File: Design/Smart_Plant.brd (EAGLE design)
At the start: 80 x 129.1 mm, 96 parts, among them IC1 TP4056, IC2 TLC555CDR, IC3 AHT20, IC4 RT9080-33GJ5, IC5 LC709203F/MH, IC6 VEML7700-TR, J6 USB-C, Q1 IRLML0100, T1 MMBT2222A, T2 LBSS84LT1G, U2 ESP32-WROOM-32, X5 ESP32-S3QFN54, Y2 40MHz

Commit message: Design V1R3
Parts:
- removed C21: 5.6pF, esp32-thing-temp:0603
- removed C46, C48, C55, C57, C62, C63: 1uF, microbuilder:_0402NO
- removed C47, C52, C53, C54, C56, C58: 0.1uF, microbuilder:_0402NO
- removed C49: 22uF, microbuilder:0805-NO
- removed C59, C60: 16pF, microbuilder:_0402NO
- removed C61: 1uF, SpaceDIY_passive_components:C0402
- removed E2: ANTENNA, esp32-thing-temp:TRACE_ANTENNA_2.4GHZ_25.7MM_TUNED
- removed IC5: LC709203F/MH, adafruit_sensor:WLCSP9
- removed J4: (no value), SpaceDIY_connectors:JST-2-SMD
- removed L2: 2.7nH, SparkFun-Passives:0603
- removed L5: 2nH, microbuilder:_0402NO
- removed R29: 0, microbuilder:_0402NO
- removed R30: 1Meg, microbuilder:_0402NO
- removed R31: 10K, SpaceDIY_passive_components:R0402
- removed U$42: (no value), itsy_silks:QTPY_ESP32_TOP
- removed U2: ESP32-WROOM-32, ESP32-WROOM-32:MODULE_ESP32-WROOM-32
- removed X5: ESP32-S3QFN54, adafruit_wireless:QFN56_7X7
- removed Y2: 40MHz, microbuilder:CRYSTAL_2X1.6
- added C12: 0.1uF, rcl:C0603
- added IC7: MAX17048G+T10, SpaceDIY_IC:SON50P200X200X80-9N
- added R36, R37: 5.1k, rcl:R0603
- added R9: 10K, rcl:R0603
- added U1: ESP32-S3-MINI-1-N8, SpaceDIY_modules:XCVR_ESP32-S3-MINI-1-N8
- C20: value 2.4pF -> 10uF; device esp32-thing-temp:0603 -> rcl:C0603
- C40: value 1uF -> 0.1uF
- FPC: device SpaceDIY_connectors:FPC-05FB-24PH20 -> SpaceDIY_connectors:FPC_24_0.5MM
- J1: device SparkFun-Connectors:1X02 -> SpaceDIY_connectors:JST-2-SMD
- moved R18 146.9 mm to (25.5, 13.4), turned to 90 degrees
- moved R14 142.0 mm to (23.4, 13.6), turned to 270 degrees
- moved C20 58.3 mm to (25.5, 27.0), turned to 180 degrees
- moved C11 42.1 mm to (15.0, 30.0)
- moved C40 34.3 mm to (22.0, 17.5)
- moved J1 20.1 mm to (5.50, 17.0)
- moved C4 14.6 mm to (11.5, 17.5), turned to 90 degrees
- moved R6 12.1 mm to (3.50, 32.5)
- moved IC1 11.7 mm to (16.0, 19.5)
- moved R4 9.85 mm to (11.5, 21.0), turned to 270 degrees
- moved C8 9.69 mm to (14.0, 13.5), turned to 90 degrees
- moved C1 9.54 mm to (11.5, 13.5), turned to 90 degrees
- moved IC6 8.06 mm to (10.0, 32.5)
- moved R5 7.68 mm to (7.00, 32.5)
- moved IC4 6.21 mm to (17.5, 13.5), turned to 0 degrees
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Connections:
- removed net !RESET: C61.1, R31.2, S2.3, X5.4
- removed net A2: X5.14
- removed net A3: X5.13
- removed net IO10_DBLTAP: C62.1, R30.2, X5.15
- removed net LIGHT: U2.9
- removed net LNA_IN1: C21.1, L2.1, X5.1
- removed net MISO: X5.42
- removed net N$53: C59.1, X5.54, Y2.3
- removed net N$54: C60.1, R29.1, Y2.1
- removed net N$55: R29.2, X5.53
- removed net NEOPIX: X5.44
- removed net NEOPIX_PWR: X5.43
- removed net SCK: X5.41
- removed net SCL1: X5.45
- removed net SDA1: X5.47
- removed net TRACE_ANT1: C20.1, C21.2, E2.ANT
- removed net VDD3P3: C47.1, L5.2, X5.2, X5.3
- removed net VDD_SPI: C54.1, C55.1, X5.29
- new net +SOL: D6.A, R20.1
- new net N$35: J6.B5, R36.2
- net 3.3V: now also C12.1, C20.1, R9.2, U1.3; no longer C46.1, C48.1, C49.1, C52.1, C53.1, C56.1, C57.1, C58.1, C63.1, L5.1, R31.1, U2.2, X5.20, X5.27, X5.46, X5.55, X5.56
- net BATTERY: now also U1.21; no longer U2.7, X5.24
- net BUSY: now also U1.28; no longer U2.10
- net D+: now also U1.24; no longer X5.26
- net D-: now also U1.23; no longer X5.25
- net DC: now also U1.33; no longer U2.12
- net DISPCS: now also U1.29; no longer U2.23
- net GND: now also C12.2, IC7.1, IC7.4, IC7.6, IC7.9, R36.1, R37.1, U1.1, U1.2, U1.42, U1.43, U1.46, U1.47, U1.48, U1.49, U1.50, U1.51, U1.52, U1.53, U1.54, U1.55, U1.56, U1.57, U1.58, U1.59, U1.60, U1.61, U1.61_1, U1.61_2, U1.61_3, U1.61_4, U1.61_5, U1.61_6, U1.61_7, U1.61_8, U1.62, U1.63, U1.64, U1.65; no longer C46.2, C47.2, C48.2, C49.2, C52.2, C53.2, C54.2, C55.2, C56.2, C57.2, C58.2, C59.2, C60.2, C61.2, C62.2, C63.2, E2.GND, E2.GND2, IC5.A1, IC5.B1, J4.2, L2.2, R30.1, U2.1, U2.15, U2.38, U2.39_1, U2.39_10, U2.39_11, U2.39_12, U2.39_13, U2.39_14, U2.39_15, U2.39_16, U2.39_17, U2.39_18, U2.39_19, U2.39_2, U2.39_20, U2.39_21, U2.39_3, U2.39_4, U2.39_5, U2.39_6, U2.39_7, U2.39_8, U2.39_9, X5.57
- net IO0: now also U1.4; no longer U2.25, X5.5
- net MOISTURE: now also U1.19; no longer U2.8, X5.23
- net MOSI: now also U1.31; no longer U2.13, X5.40
- net N$46: now also J6.A5, R37.2; no longer D6.A, J1.1, R20.1
- net RESET: now also U1.34; no longer U2.11
- net RST: now also R9.1, S2.3, U1.45; no longer U2.3
- net RX: now also U1.40; no longer U2.34, X5.50
- net SCL: now also IC7.7, U1.8; no longer IC5.C2, U2.36, X5.11
- net SCLK: now also U1.32; no longer U2.16
- net SDA: now also IC7.8, U1.7; no longer IC5.C1, U2.33, X5.12
- net SENS: now also U1.25; no longer U2.27, X5.9
- net TX: now also U1.39; no longer U2.35, X5.49
- net VBAT: now also IC7.2, IC7.3, J1.1; no longer IC5.A3, J4.1
- net VSOLAR: now also U1.20; no longer U2.6
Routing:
- net VSENS: track 69.3 -> 125.7 mm, vias 4 -> 5
- net SCL: track 19.1 -> 64.3 mm, vias 0 -> 5
- net SDA: track 18.4 -> 61.7 mm, vias 0 -> 5
- net D+: track 0.00 -> 40.1 mm, vias 0 -> 2
- net D-: track 0.00 -> 39.3 mm, vias 0 -> 2
- net RST: track 59.5 -> 34.1 mm
- net N$1: track 2.86 -> 26.2 mm, vias 0 -> 2
- net N$6: track 2.29 -> 23.3 mm, vias 0 -> 2
- net DC: track 48.7 -> 30.8 mm
- net RESET: track 47.5 -> 29.7 mm
- net N$3: track 19.2 -> 2.00 mm, vias 2 -> 0
- net SCLK: track 42.5 -> 25.5 mm
- net MOSI: track 42.3 -> 25.3 mm
- net GND: track 12.3 -> 26.9 mm, vias 73 -> 40
- net VIN: track 48.7 -> 62.8 mm, vias 3 -> 4
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- added copper zone on layer 1, net +SOL
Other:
- board text added: "V1R3"
- board text removed: "+"
- board text removed: "-"
- board text removed: "V1R2"

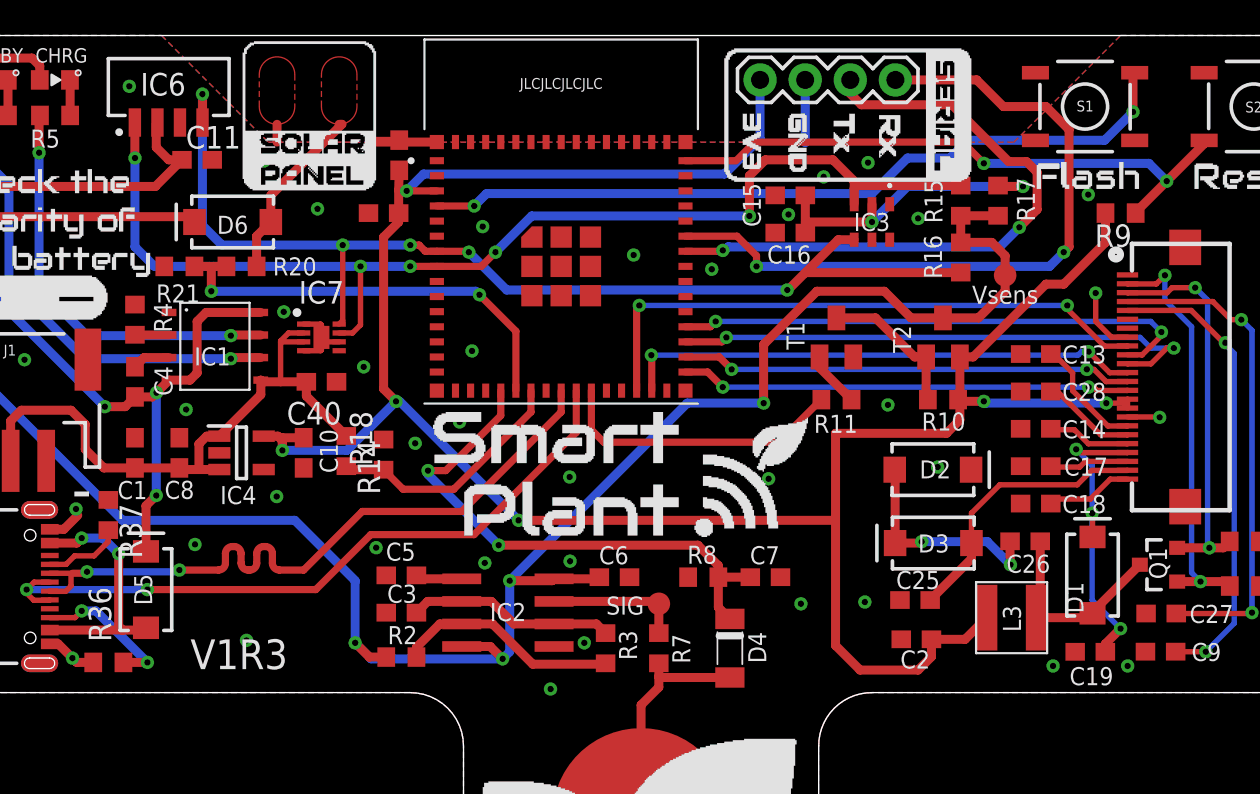
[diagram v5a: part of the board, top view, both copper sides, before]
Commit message: First draft of the V2R1 design
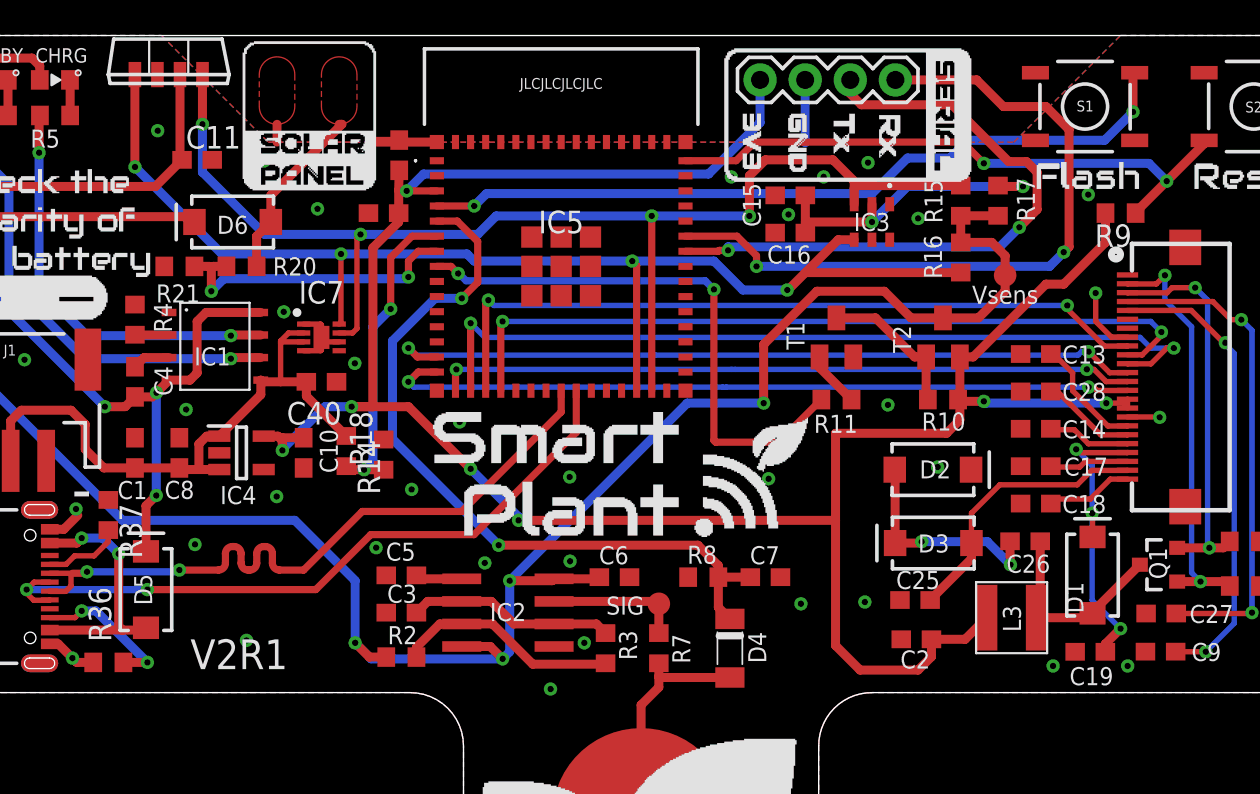
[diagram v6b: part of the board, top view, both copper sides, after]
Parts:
- removed U1: ESP32-S3-MINI-1-N8, SpaceDIY_modules:XCVR_ESP32-S3-MINI-1-N8
- added IC5: ESP32-S2-MINI-1-N4R2, SpaceDIY_modules:ESP32S2MINI1N4R2
- IC6: device SpaceDIY_sensors:VEML7700 -> SpaceDIY_sensors:VEML7700-TR
- moved IC6 2.00 mm to (10.0, 34.5)
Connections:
- net 3.3V: now also IC5.3; no longer U1.3
- net BATTERY: now also IC5.6; no longer U1.21
- net BUSY: now also IC5.18; no longer U1.28
- net D+: now also IC5.24; no longer U1.24
- net D-: now also IC5.23; no longer U1.23
- net DC: now also IC5.17; no longer U1.33
- net DISPCS: now also IC5.14; no longer U1.29
- net GND: now also IC5.1, IC5.2, IC5.30, IC5.42, IC5.43, IC5.46, IC5.47, IC5.48, IC5.49, IC5.50, IC5.51, IC5.52, IC5.53, IC5.54, IC5.55, IC5.56, IC5.57, IC5.58, IC5.59, IC5.60, IC5.61, IC5.62, IC5.63, IC5.64, IC5.65, IC5.66, IC5.67, IC5.68, IC5.69, IC5.70, IC5.71, IC5.72, IC5.73; no longer U1.1, U1.2, U1.42, U1.43, U1.46, U1.47, U1.48, U1.49, U1.50, U1.51, U1.52, U1.53, U1.54, U1.55, U1.56, U1.57, U1.58, U1.59, U1.60, U1.61, U1.61_1, U1.61_2, U1.61_3, U1.61_4, U1.61_5, U1.61_6, U1.61_7, U1.61_8, U1.62, U1.63, U1.64, U1.65
- net IO0: now also IC5.4; no longer U1.4
- net MOISTURE: now also IC5.5; no longer U1.19
- net MOSI: now also IC5.15; no longer U1.31
- net RESET: now also IC5.19; no longer U1.34
- net RST: now also IC5.45; no longer U1.45
- net RX: now also IC5.40; no longer U1.40
- net SCL: now also IC5.29; no longer U1.8
- net SCLK: now also IC5.16; no longer U1.32
- net SDA: now also IC5.28; no longer U1.7
- net SENS: now also IC5.8; no longer U1.25
- net TX: now also IC5.39; no longer U1.39
- net VSOLAR: now also IC5.7; no longer U1.20
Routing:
- net MOSI: track 25.3 -> 42.5 mm
- net DC: track 30.8 -> 47.0 mm
- net SENS: track 16.4 -> 31.7 mm, vias 0 -> 2
- net RESET: track 29.7 -> 43.9 mm
- net SCLK: track 25.5 -> 39.3 mm
- net DISPCS: track 29.4 -> 43.0 mm
- net MOISTURE: track 30.5 -> 43.1 mm
- net BUSY: track 33.4 -> 42.3 mm
- net SDA: track 61.7 -> 69.9 mm, vias 5 -> 4
- net VSOLAR: track 24.6 -> 17.3 mm
- net SCL: track 64.3 -> 70.9 mm, vias 5 -> 4
- net BATTERY: track 13.9 -> 17.9 mm, vias 0 -> 2
- net VSENS: track 125.7 -> 127.4 mm
- net 3.3V: track 135.4 -> 136.2 mm, vias 6 -> 7
- net GND: vias 40 -> 37
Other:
- board text added: "V2R1"
- board text removed: "V1R3"
